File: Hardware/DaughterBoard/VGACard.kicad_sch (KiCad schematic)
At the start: 17 parts, among them J6 VGA_OUT, U2 ATmega1284P-PU, U4 ATmega328P-PU, U5 HM62256BLP, U6 74LS365, X1 ACO-20MHz

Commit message: Fix PPU
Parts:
- R12, R14, R16: value 680 -> 1.5K
- R13, R15, R17: value 1.5K -> 680
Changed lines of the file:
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@@
   (junction (at 142.24 85.725) (diameter 1.016) (color 0 0 0 0))
   (junction (at 142.24 88.9) (diameter 1.016) (color 0 0 0 0))
+  (no_connect (at 266.065 58.42))
+  (no_connect (at 54.61 135.89))
+  (no_connect (at 54.61 113.03))
+  (no_connect (at 250.825 45.72))
+  (no_connect (at 122.555 121.285))
+  (no_connect (at 122.555 116.205))
+  (no_connect (at 250.825 43.18))
+  (no_connect (at 266.065 53.34))
   (no_connect (at 266.065 38.1))
-  (no_connect (at 122.555 116.205))
-  (no_connect (at 250.825 45.72))
-  (no_connect (at 266.065 53.34))
-  (no_connect (at 54.61 113.03))
   (no_connect (at 24.13 105.41))
-  (no_connect (at 54.61 135.89))
-  (no_connect (at 266.065 58.42))
-  (no_connect (at 250.825 43.18))
-  (no_connect (at 122.555 121.285))
   (bus_entry (at 70.485 95.25) (size 2.54 2.54)
     (stroke (width 0.1524) (type solid) (color 0 0 0 0))
@@
     (in_bom yes) (on_board yes)
     (property "Reference" "R12" (id 0) (at 198.12 26.67 90))
-    (property "Value" "680" (id 1) (at 204.47 29.21 90))
+    (property "Value" "1.5K" (id 1) (at 204.47 29.21 90))
     (property "Footprint" "Resistor_THT:R_Axial_DIN0207_L6.3mm_D2.5mm_P10.16mm_Horizontal" (id 2) (at 198.12 27.432 90)
       (effects (font (size 1.27 1.27)) hide)
@@
     (in_bom yes) (on_board yes)
     (property "Reference" "R13" (id 0) (at 198.12 35.56 90))
-    (property "Value" "1.5K" (id 1) (at 205.105 38.1 90))
+    (property "Value" "680" (id 1) (at 205.105 38.1 90))
     (property "Footprint" "Resistor_THT:R_Axial_DIN0207_L6.3mm_D2.5mm_P10.16mm_Horizontal" (id 2) (at 198.12 36.322 90)
       (effects (font (size 1.27 1.27)) hide)
@@
     (in_bom yes) (on_board yes)
     (property "Reference" "R14" (id 0) (at 198.12 45.085 90))
-    (property "Value" "680" (id 1) (at 204.47 47.625 90))
+    (property "Value" "1.5K" (id 1) (at 204.47 47.625 90))
     (property "Footprint" "Resistor_THT:R_Axial_DIN0207_L6.3mm_D2.5mm_P10.16mm_Horizontal" (id 2) (at 198.12 45.847 90)
       (effects (font (size 1.27 1.27)) hide)
@@
     (in_bom yes) (on_board yes)
     (property "Reference" "R15" (id 0) (at 198.12 53.34 90))
-    (property "Value" "1.5K" (id 1) (at 205.105 55.88 90))
+    (property "Value" "680" (id 1) (at 205.105 55.88 90))
     (property "Footprint" "Resistor_THT:R_Axial_DIN0207_L6.3mm_D2.5mm_P10.16mm_Horizontal" (id 2) (at 198.12 54.102 90)
       (effects (font (size 1.27 1.27)) hide)
@@
     (in_bom yes) (on_board yes)
     (property "Reference" "R16" (id 0) (at 198.755 61.595 90))
-    (property "Value" "680" (id 1) (at 205.105 64.135 90))
+    (property "Value" "1.5K" (id 1) (at 205.105 64.135 90))
     (property "Footprint" "Resistor_THT:R_Axial_DIN0207_L6.3mm_D2.5mm_P10.16mm_Horizontal" (id 2) (at 198.755 62.357 90)
       (effects (font (size 1.27 1.27)) hide)
@@
     (in_bom yes) (on_board yes)
     (property "Reference" "R17" (id 0) (at 198.755 69.85 90))
-    (property "Value" "1.5K" (id 1) (at 205.74 72.39 90))
+    (property "Value" "680" (id 1) (at 205.74 72.39 90))
     (property "Footprint" "Resistor_THT:R_Axial_DIN0207_L6.3mm_D2.5mm_P10.16mm_Horizontal" (id 2) (at 198.755 70.612 90)
       (effects (font (size 1.27 1.27)) hide)

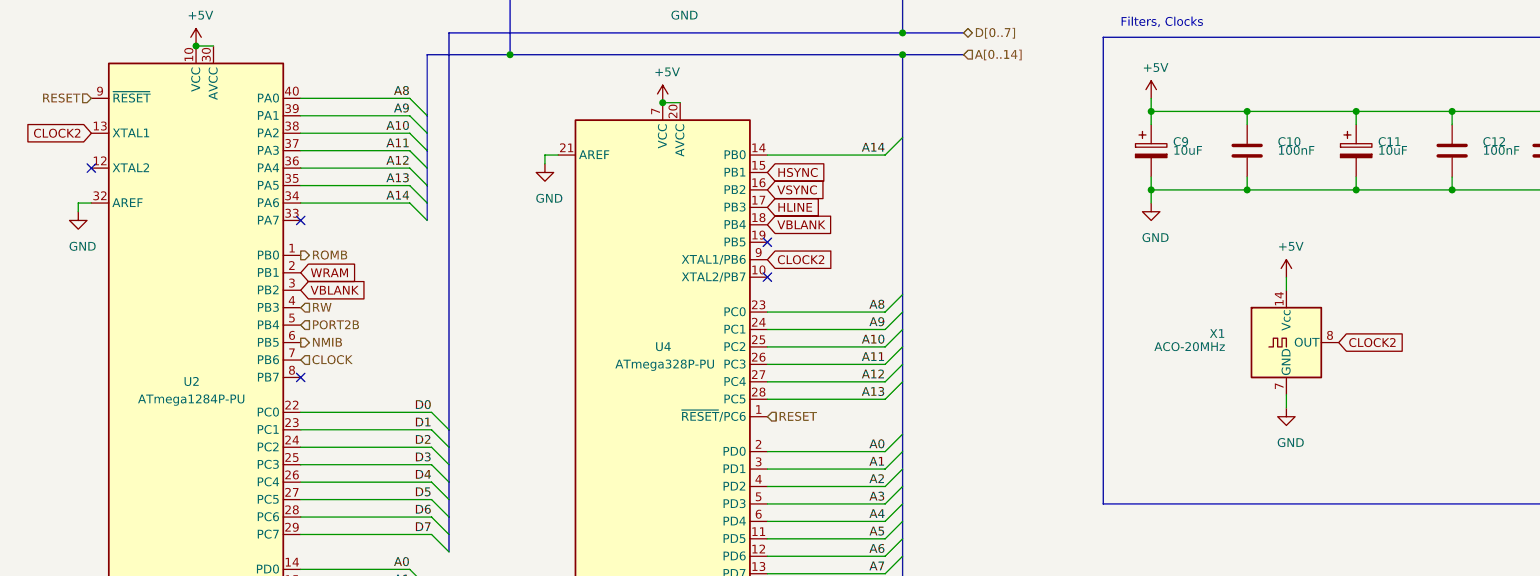
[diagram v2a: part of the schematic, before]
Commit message: Implement APU and fix schematics
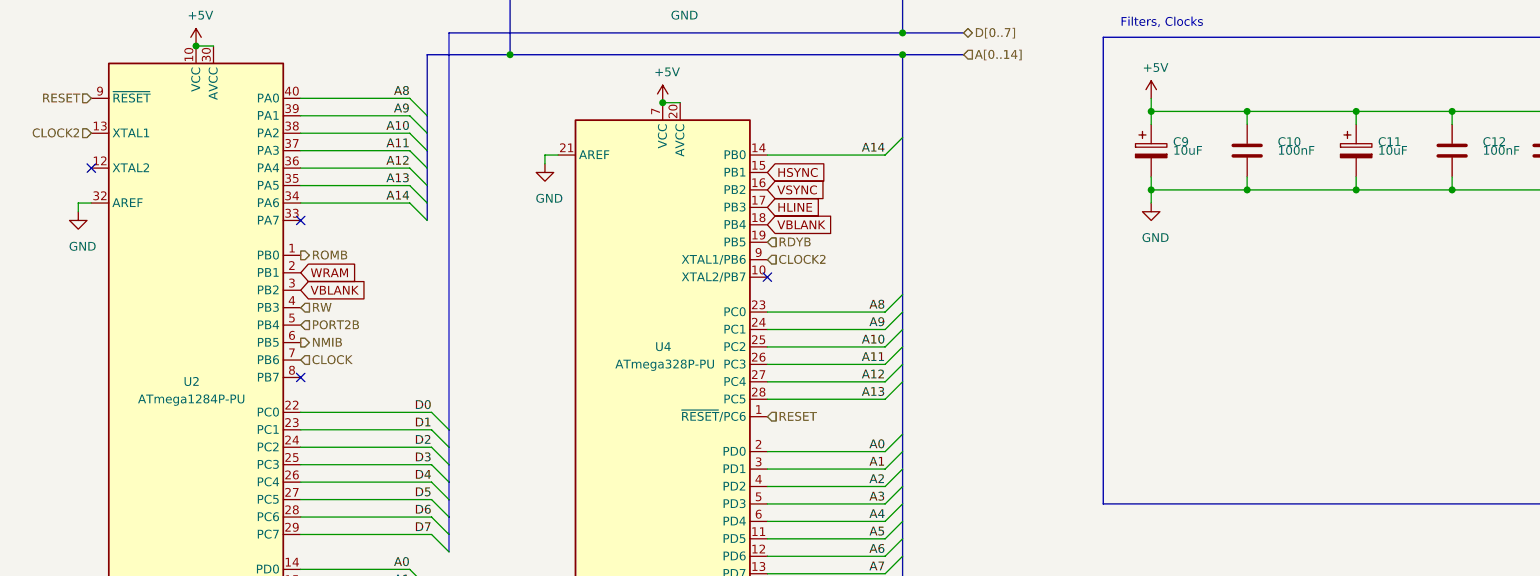
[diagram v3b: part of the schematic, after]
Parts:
- removed X1: ACO-20MHz, Oscillator:Oscillator_DIP-14, symbol Oscillator:ACO-xxxMHz
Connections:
- net RDYB: now reaches U4.19 (PB5)
- no-connect marks 10 -> 9
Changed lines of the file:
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@@
   (junction (at 142.24 85.725) (diameter 1.016) (color 0 0 0 0))
   (junction (at 142.24 88.9) (diameter 1.016) (color 0 0 0 0))
+  (no_connect (at 266.065 53.34))
+  (no_connect (at 122.555 121.285))
+  (no_connect (at 54.61 135.89))
+  (no_connect (at 250.825 45.72))
+  (no_connect (at 24.13 105.41))
+  (no_connect (at 250.825 43.18))
+  (no_connect (at 54.61 113.03))
   (no_connect (at 266.065 58.42))
-  (no_connect (at 54.61 135.89))
-  (no_connect (at 54.61 113.03))
-  (no_connect (at 250.825 45.72))
-  (no_connect (at 122.555 121.285))
-  (no_connect (at 122.555 116.205))
-  (no_connect (at 250.825 43.18))
-  (no_connect (at 266.065 53.34))
   (no_connect (at 266.065 38.1))
-  (no_connect (at 24.13 105.41))
   (bus_entry (at 70.485 95.25) (size 2.54 2.54)
     (stroke (width 0.1524) (type solid) (color 0 0 0 0))
@@
     (stroke (width 0) (type solid) (color 0 0 0 0))
   )
-  (wire (pts (xy 198.12 121.285) (xy 198.12 123.19))
-    (stroke (width 0) (type solid) (color 0 0 0 0))
-  )
-  (wire (pts (xy 198.12 138.43) (xy 198.12 140.335))
-    (stroke (width 0) (type solid) (color 0 0 0 0))
-  )
   (wire (pts (xy 201.93 29.21) (xy 201.93 33.655))
     (stroke (width 0) (type solid) (color 0 0 0 0))
@@
     (effects (font (size 1.27 1.27)) (justify right bottom))
   )
-  (global_label "CLOCK2" (shape input) (at 24.13 100.33 180)    (property "Intersheet References" "${INTERSHEET_REFS}" (id 0) (at 12.8148 100.2506 0)
-      (effects (font (size 1.27 1.27)) (justify right) hide)
+  (global_label "WRAM" (shape input) (at 54.61 120.65 0)    (property "Intersheet References" "${INTERSHEET_REFS}" (id 0) (at -1.27 3.81 0)
+      (effects (font (size 1.27 1.27)) hide)
+    )
+    (effects (font (size 1.27 1.27)) (justify left))
+  )
+  (global_label "VBLANK" (shape input) (at 54.61 123.19 0)    (property "Intersheet References" "${INTERSHEET_REFS}" (id 0) (at -1.27 3.81 0)
+      (effects (font (size 1.27 1.27)) hide)
+    )
+    (effects (font (size 1.27 1.27)) (justify left))
+  )
+  (global_label "HLINE" (shape input) (at 122.555 65.405 0)    (property "Intersheet References" "${INTERSHEET_REFS}" (id 0) (at -1.27 3.81 0)
+      (effects (font (size 1.27 1.27)) hide)
+    )
+    (effects (font (size 1.27 1.27)) (justify left))
+  )
+  (global_label "WRAM" (shape input) (at 122.555 67.945 0)    (property "Intersheet References" "${INTERSHEET_REFS}" (id 0) (at -1.27 3.81 0)
+      (effects (font (size 1.27 1.27)) hide)
+    )
+    (effects (font (size 1.27 1.27)) (justify left))
+  )
+  (global_label "HSYNC" (shape input) (at 122.555 106.045 0)    (property "Intersheet References" "${INTERSHEET_REFS}" (id 0) (at -1.27 3.81 0)
+      (effects (font (size 1.27 1.27)) hide)
+    )
+    (effects (font (size 1.27 1.27)) (justify left))
+  )
+  (global_label "VSYNC" (shape input) (at 122.555 108.585 0)    (property "Intersheet References" "${INTERSHEET_REFS}" (id 0) (at -1.27 3.81 0)
+      (effects (font (size 1.27 1.27)) hide)
+    )
+    (effects (font (size 1.27 1.27)) (justify left))
+  )
+  (global_label "HLINE" (shape input) (at 122.555 111.125 0)    (property "Intersheet References" "${INTERSHEET_REFS}" (id 0) (at -1.27 3.81 0)
+      (effects (font (size 1.27 1.27)) hide)
+    )
+    (effects (font (size 1.27 1.27)) (justify left))
+  )
+  (global_label "VBLANK" (shape input) (at 122.555 113.665 0)    (property "Intersheet References" "${INTERSHEET_REFS}" (id 0) (at -1.27 3.81 0)
+      (effects (font (size 1.27 1.27)) hide)
+    )
+    (effects (font (size 1.27 1.27)) (justify left))
+  )
+  (global_label "HLINE" (shape input) (at 157.48 55.245 180)    (property "Intersheet References" "${INTERSHEET_REFS}" (id 0) (at 281.305 162.56 0)
+      (effects (font (size 1.27 1.27)) hide)
     )
     (effects (font (size 1.27 1.27)) (justify right))
   )
-  (global_label "WRAM" (shape input) (at 54.61 120.65 0)    (property "Intersheet References" "${INTERSHEET_REFS}" (id 0) (at -1.27 3.81 0)
-      (effects (font (size 1.27 1.27)) hide)
-    )
-    (effects (font (size 1.27 1.27)) (justify left))
-  )
-  (global_label "VBLANK" (shape input) (at 54.61 123.19 0)    (property "Intersheet References" "${INTERSHEET_REFS}" (id 0) (at -1.27 3.81 0)
-      (effects (font (size 1.27 1.27)) hide)
-    )
-    (effects (font (size 1.27 1.27)) (justify left))
-  )
-  (global_label "HLINE" (shape input) (at 122.555 65.405 0)    (property "Intersheet References" "${INTERSHEET_REFS}" (id 0) (at -1.27 3.81 0)
-      (effects (font (size 1.27 1.27)) hide)
-    )
-    (effects (font (size 1.27 1.27)) (justify left))
-  )
-  (global_label "WRAM" (shape input) (at 122.555 67.945 0)    (property "Intersheet References" "${INTERSHEET_REFS}" (id 0) (at -1.27 3.81 0)
-      (effects (font (size 1.27 1.27)) hide)
-    )
-    (effects (font (size 1.27 1.27)) (justify left))
-  )
-  (global_label "HSYNC" (shape input) (at 122.555 106.045 0)    (property "Intersheet References" "${INTERSHEET_REFS}" (id 0) (at -1.27 3.81 0)
-      (effects (font (size 1.27 1.27)) hide)
-    )
-    (effects (font (size 1.27 1.27)) (justify left))
-  )
-  (global_label "VSYNC" (shape input) (at 122.555 108.585 0)    (property "Intersheet References" "${INTERSHEET_REFS}" (id 0) (at -1.27 3.81 0)
-      (effects (font (size 1.27 1.27)) hide)
-    )
-    (effects (font (size 1.27 1.27)) (justify left))
-  )
-  (global_label "HLINE" (shape input) (at 122.555 111.125 0)    (property "Intersheet References" "${INTERSHEET_REFS}" (id 0) (at -1.27 3.81 0)
-      (effects (font (size 1.27 1.27)) hide)
-    )
-    (effects (font (size 1.27 1.27)) (justify left))
-  )
-  (global_label "VBLANK" (shape input) (at 122.555 113.665 0)    (property "Intersheet References" "${INTERSHEET_REFS}" (id 0) (at -1.27 3.81 0)
-      (effects (font (size 1.27 1.27)) hide)
-    )
-    (effects (font (size 1.27 1.27)) (justify left))
-  )
-  (global_label "CLOCK2" (shape input) (at 122.555 118.745 0)    (property "Intersheet References" "${INTERSHEET_REFS}" (id 0) (at 133.8702 118.6656 0)
-      (effects (font (size 1.27 1.27)) (justify left) hide)
-    )
-    (effects (font (size 1.27 1.27)) (justify left))
-  )
-  (global_label "HLINE" (shape input) (at 157.48 55.245 180)    (property "Intersheet References" "${INTERSHEET_REFS}" (id 0) (at 281.305 162.56 0)
-      (effects (font (size 1.27 1.27)) hide)
-    )
-    (effects (font (size 1.27 1.27)) (justify right))
-  )
   (global_label "BLUE" (shape input) (at 203.835 33.655 0)    (property "Intersheet References" "${INTERSHEET_REFS}" (id 0) (at -1.27 3.81 0)
       (effects (font (size 1.27 1.27)) hide)
@@
   (global_label "RED" (shape input) (at 204.47 68.58 0)    (property "Intersheet References" "${INTERSHEET_REFS}" (id 0) (at -1.27 3.81 0)
       (effects (font (size 1.27 1.27)) hide)
-    )
-    (effects (font (size 1.27 1.27)) (justify left))
-  )
-  (global_label "CLOCK2" (shape input) (at 205.74 130.81 0)    (property "Intersheet References" "${INTERSHEET_REFS}" (id 0) (at 217.0552 130.7306 0)
-      (effects (font (size 1.27 1.27)) (justify left) hide)
     )
     (effects (font (size 1.27 1.27)) (justify left))
@@
     (effects (font (size 1.27 1.27)) (justify right))
   )
+  (hierarchical_label "CLOCK2" (shape input) (at 24.13 100.33 180)
+    (effects (font (size 1.27 1.27)) (justify right))
+  )
   (hierarchical_label "ROMB" (shape output) (at 54.61 118.11 0)
     (effects (font (size 1.27 1.27)) (justify left))
@@
   )
   (hierarchical_label "CLOCK" (shape input) (at 54.61 133.35 0)
+    (effects (font (size 1.27 1.27)) (justify left))
+  )
+  (hierarchical_label "RDYB" (shape input) (at 122.555 116.205 0)
+    (effects (font (size 1.27 1.27)) (justify left))
+  )
+  (hierarchical_label "CLOCK2" (shape input) (at 122.555 118.745 0)
     (effects (font (size 1.27 1.27)) (justify left))
   )
@@
     )
   )
-  (symbol (lib_id "power:+5V") (at 198.12 121.285 0) (unit 1)
-    (in_bom yes) (on_board yes)
-    (property "Reference" "#PWR033" (id 0) (at 198.12 125.095 0)
-      (effects (font (size 1.27 1.27)) hide)
-    )
-    (property "Value" "+5V" (id 1) (at 198.755 116.84 0))
-    (property "Footprint" "" (id 2) (at 198.12 121.285 0)
-      (effects (font (size 1.27 1.27)) hide)
-    )
-    (property "Datasheet" "" (id 3) (at 198.12 121.285 0)
-      (effects (font (size 1.27 1.27)) hide)
-    )
-  )
   (symbol (lib_id "power:GND") (at 22.225 111.76 0) (unit 1)
     (in_bom yes) (on_board yes)
@@
     )
     (property "Datasheet" "" (id 3) (at 178.435 110.49 0)
-      (effects (font (size 1.27 1.27)) hide)
-    )
-  )
-  (symbol (lib_id "power:GND") (at 198.12 140.335 0) (unit 1)
-    (in_bom yes) (on_board yes)
-    (property "Reference" "#PWR034" (id 0) (at 198.12 146.685 0)
-      (effects (font (size 1.27 1.27)) hide)
-    )
-    (property "Value" "GND" (id 1) (at 198.755 145.415 0))
-    (property "Footprint" "" (id 2) (at 198.12 140.335 0)
-      (effects (font (size 1.27 1.27)) hide)
-    )
-    (property "Datasheet" "" (id 3) (at 198.12 140.335 0)
       (effects (font (size 1.27 1.27)) hide)
     )
@@
       (effects (font (size 1.27 1.27)) hide)
     )
-  )
-  (symbol (lib_id "Oscillator:ACO-xxxMHz") (at 198.12 130.81 0) (unit 1)
-    (in_bom yes) (on_board yes)
-    (property "Reference" "X1" (id 0) (at 189.23 129.54 0)
-      (effects (font (size 1.27 1.27)) (justify right))
-    )
-    (property "Value" "ACO-20MHz" (id 1) (at 189.23 131.445 0)
-      (effects (font (size 1.27 1.27)) (justify right))
-    )
-    (property "Footprint" "Oscillator:Oscillator_DIP-14" (id 2) (at 209.55 139.7 0)
-      (effects (font (size 1.27 1.27)) hide)
-    )
-    (property "Datasheet" "" (id 3) (at 195.58 130.81 0)
-      (effects (font (size 1.27 1.27)) hide)
-    )

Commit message: Version 1.2
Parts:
- U5: value HM62256BLP -> AS6C62256
- U6: value 74LS365 -> 74HC365
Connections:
- net ROMB is gone; now on net RDYB: U2.1 (PB0)
- net RDYB: no longer U4.19 (PB5)
- net A15: now reaches U2.33 (PA7)
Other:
- moved on the sheet: R14, R16, R17
